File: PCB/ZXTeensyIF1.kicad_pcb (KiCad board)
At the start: 2 copper layers, 222.4 x 72.5 mm, 79 parts, among them Q1 BC213C, Q10 ZTX313, Q11 ZTX313, Q2 BC213C, Q3 BC184C, Q4 PN2222A, Q5 PN2222A, Q6 BC184C, Q9 BC184C, SW1 PTH_RA_h7.5mm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

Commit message: feat: Upload initial PCB v0.3
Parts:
- C3, C4: footprint Resistor_THT:R_Axial_DIN0207_L6.3mm_D2.5mm_P10.16mm_Horizontal -> Capacitor_THT:C_Disc_D3.4mm_W2.1mm_P2.50mm
- Q4, Q5: footprint Package_TO_SOT_THT:TO-92_Inline -> Package_TO_SOT_THT:TO-92_Inline_Wide
- R35: footprint Resistor_THT:R_Axial_DIN0207_L6.3mm_D2.5mm_P10.16mm_Horizontal -> Resistor_THT:R_Axial_DIN0207_L6.3mm_D2.5mm_P7.62mm_Horizontal
- moved C3 10.5 mm to (150.3, 112.8), turned to -90 degrees
- moved R35 9.34 mm to (143.7, 112.8), turned to -90 degrees
- moved C4 3.61 mm to (147.6, 115.3), turned to -90 degrees
- moved C1 2.24 mm to (124.8, 82.0), turned to -90 degrees
- moved C7 1.46 mm to (96.2, 82.9)
- moved Q5 1.09 mm to (176.6, 115.3)
- moved C8 0.79 mm to (93.6, 94.5)
- moved C13 0.76 mm to (128.1, 95.0)
- moved Q4 0.73 mm to (178.9, 115.3)
- moved X1 0.26 mm to (154.2, 117.7)
- moved C2 0.10 mm to (124.8, 87.7)
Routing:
- net GND: track 867.7 -> 837.8 mm, vias 30 -> 32
- net Net-(C3-Pad1): track 77.5 -> 67.9 mm
- net Net-(U8-VS-): track 27.5 -> 19.1 mm
- net ~{RESET}: track 141.6 -> 135.7 mm
- net ~{NMI}: track 78.0 -> 83.5 mm
- net -5V: track 12.4 -> 7.11 mm
- net Net-(C4-Pad2): track 78.0 -> 72.9 mm
- net DTR_1: track 153.3 -> 149.5 mm
- net D7: track 158.3 -> 161.8 mm
- net +9V: track 143.7 -> 141.1 mm
- net D1: track 189.7 -> 187.2 mm
- net Net-(U8-T1OUT): track 48.0 -> 50.3 mm
- net D2: track 172.0 -> 170.4 mm
- net Net-(U8-VS+): track 22.8 -> 21.4 mm
- net D4: track 168.6 -> 170.0 mm
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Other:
- board text added: "${PRJ_NAME} ${PRJ_REVISION}, CraigE ${PRJ_DATE}"
- board text removed: "ZXTeensyIF1 v0.1, CraigE 2025"

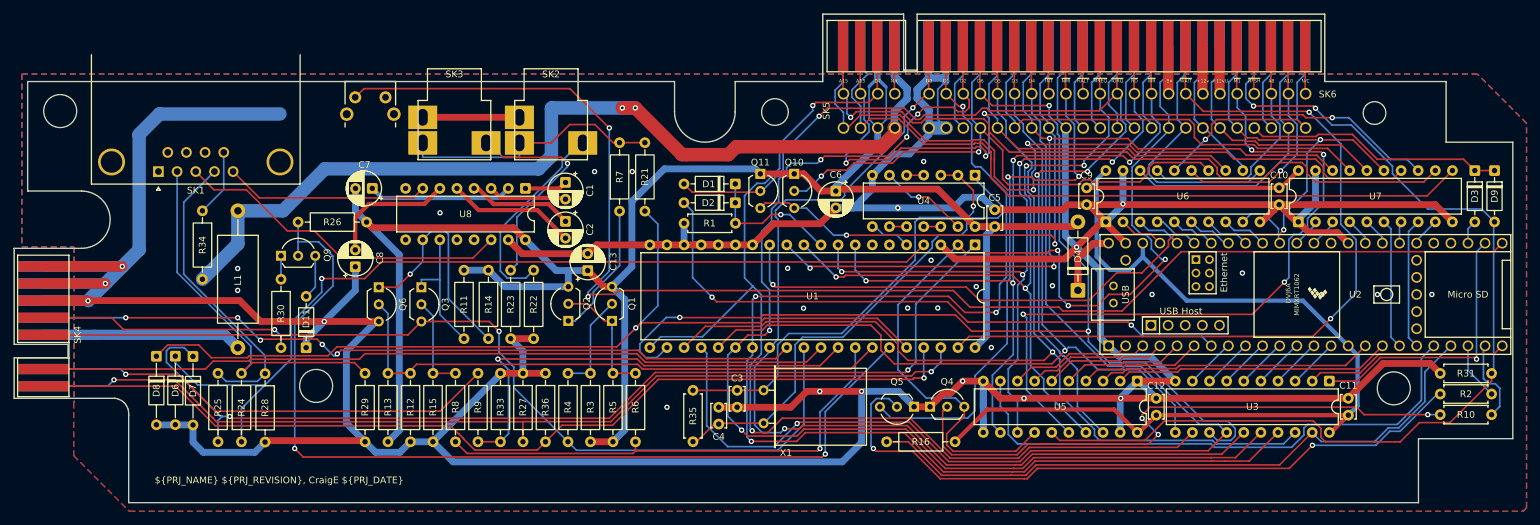
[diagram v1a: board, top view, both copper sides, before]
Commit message: feat: Add ESP-01S header to PCB v0.5
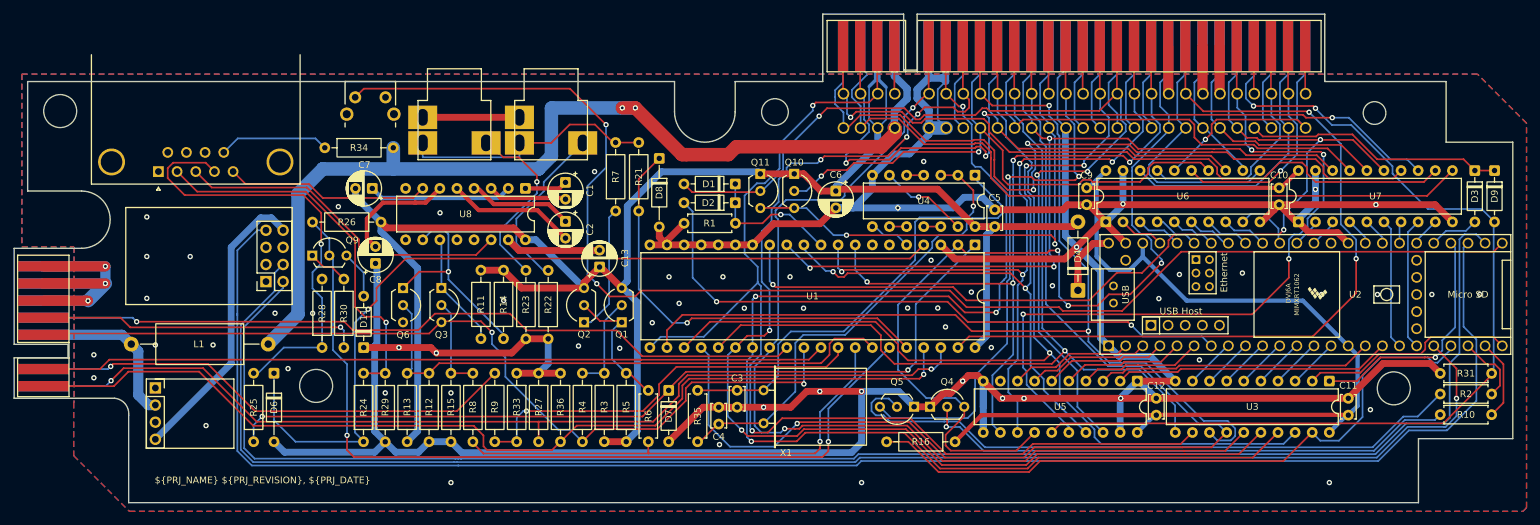
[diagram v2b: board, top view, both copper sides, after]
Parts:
- added J1: ESP-01S-Header, Connector_PinSocket_2.54mm:PinSocket_2x04_P2.54mm_Vertical, F.Cu at (80.4, 96.7)
- added J3: Polou D24V5F3, Connector_PinSocket_2.54mm:PinSocket_1x04_P2.54mm_Vertical, F.Cu at (64.0, 112.5)
- D7: footprint Diode_THT:D_DO-35_SOD27_P10.16mm_Horizontal -> Diode_THT:D_DO-35_SOD27_P7.62mm_Horizontal
- R6: footprint Resistor_THT:R_Axial_DIN0207_L6.3mm_D2.5mm_P10.16mm_Horizontal -> Resistor_THT:R_Axial_DIN0207_L6.3mm_D2.5mm_P7.62mm_Horizontal
- moved D8 80.2 mm to (138.7, 78.4)
- moved D7 70.8 mm to (140.1, 112.8)
- moved R34 20.4 mm to (89.1, 76.8), turned to 0 degrees
- moved L1 20.3 mm to (80.7, 106.0), turned to 180 degrees
- moved R24 18.1 mm to (94.8, 120.4)
- moved D6 14.9 mm to (81.6, 110.3)
- moved R30 9.33 mm to (91.9, 96.3)
- moved R28 9.30 mm to (88.7, 106.5), turned to 90 degrees
- moved D11 8.53 mm to (94.9, 106.5)
- moved R25 5.28 mm to (78.5, 120.4)
- moved Q9 4.64 mm to (87.2, 92.8)
- moved Q6 3.60 mm to (100.7, 97.6)
- moved R6 3.16 mm to (137.1, 112.8)
- moved C8 3.04 mm to (96.6, 94.0)
- moved R29 3.00 mm to (98.1, 110.3)
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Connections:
- net Net-(SK4-Pin_B4) renamed +9V0
- U2 pad 20: TIN_A -> TEPD
- U2 pad 26: TDDir -> TERX
- U2 pad 27: Net-(D3-A) -> TETX
- U2 pad 28: unconnected-(U2-36_CS-Pad28) -> TDDir
- U2 pad 29: unconnected-(U2-37_CS-Pad29) -> Net-(D3-A)
- U5 pad 9: TIN_A -> unconnected-(U5-A8-Pad9)
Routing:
- net TETX: track 0.00 -> 248.5 mm
- net TERX: track 0.00 -> 240.9 mm
- net TEPD: track 0.00 -> 225.9 mm, vias 0 -> 1
- net GND: track 837.8 -> 726.8 mm, vias 32 -> 65
- net TIN_A: track 82.8 -> 0.00 mm
- net NET36: track 136.5 -> 64.6 mm
- net Net-(J1-Pin_8): track 0.00 -> 43.5 mm
- net DTR_1: track 149.5 -> 125.8 mm
- net Net-(R25-Pad2): track 44.8 -> 67.5 mm, vias 0 -> 1
- net ERASE_35: track 141.1 -> 127.3 mm
- net Net-(SK4-Pin_A5): track 38.1 -> 47.9 mm
- net Net-(Q4-B): track 88.9 -> 80.0 mm, vias 3 -> 1
- net D6: track 163.8 -> 155.3 mm, vias 3 -> 2
- net WRPROT_32: track 68.8 -> 60.4 mm
- net Net-(Q5-B): track 102.6 -> 95.7 mm, vias 2 -> 0
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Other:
- board text added: "${PRJ_NAME} ${PRJ_REVISION}, ${PRJ_DATE}"
- board text removed: "${PRJ_NAME} ${PRJ_REVISION}, CraigE ${PRJ_DATE}"

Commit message: Add silkscreen text
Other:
- board text added: "3V3"
- board text added: "ESP-01S"
- board text added: "GND"
- board text added: "VIN"
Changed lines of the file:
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@@
 		)
 	)
-	(property "PRJ_DATE" "2026-02-05")
+	(property "PRJ_DATE" "2026-02-08")
 	(property "PRJ_NAME" "ZXTeensyIF1")
 	(property "PRJ_REVISION" "v0.5")
@@
 		(layer "Edge.Cuts")
 	)
+	(gr_text "3V3"
+		(at 65.8114 120.6754 0)
+		(layer "F.SilkS")
+		(effects
+			(font
+				(size 1 1)
+				(thickness 0.15)
+			)
+			(justify left bottom)
+		)
+	)
+	(gr_text "VIN"
+		(at 65.8114 115.5954 0)
+		(layer "F.SilkS")
+		(effects
+			(font
+				(size 1 1)
+				(thickness 0.15)
+			)
+			(justify left bottom)
+		)
+	)
+	(gr_text "GND"
+		(at 65.8114 118.1354 0)
+		(layer "F.SilkS")
+		(effects
+			(font
+				(size 1 1)
+				(thickness 0.15)
+			)
+			(justify left bottom)
+		)
+	)
+	(gr_text "ESP-01S"
+		(locked yes)
+		(at 68.51071 89.66955 0)
+		(layer "F.SilkS")
+		(effects
+			(font
+				(size 1 1)
+				(thickness 0.15)
+			)
+			(justify left bottom)
+		)
+	)
 	(gr_text "${PRJ_NAME} ${PRJ_REVISION}, ${PRJ_DATE}"
 		(at 63.8556 126.746 0)
@@
 	(group ""
 		(locked yes)
-		(members "d820edde-8ae0-4da0-8973-3ad2fe5a2ae9" "de12b274-2a6e-492c-b6fc-8a5622de27ed")
+		(members "d820edde-8ae0-4da0-8973-3ad2fe5a2ae9" "de12b274-2a6e-492c-b6fc-8a5622de27ed"
+			"e628a1bc-3ac2-4b91-a549-73b6a515b474"
+		)
+	)
+	(group ""
+		(members "3c47943e-7347-4d15-bad2-3ed72209b964" "80866c92-00ea-4d94-bf1f-d6b2a7ca4847"
+			"d6e526b1-69ad-4888-899b-9402fcfd270b"
+		)
 	)
 	(embedded_fonts no)

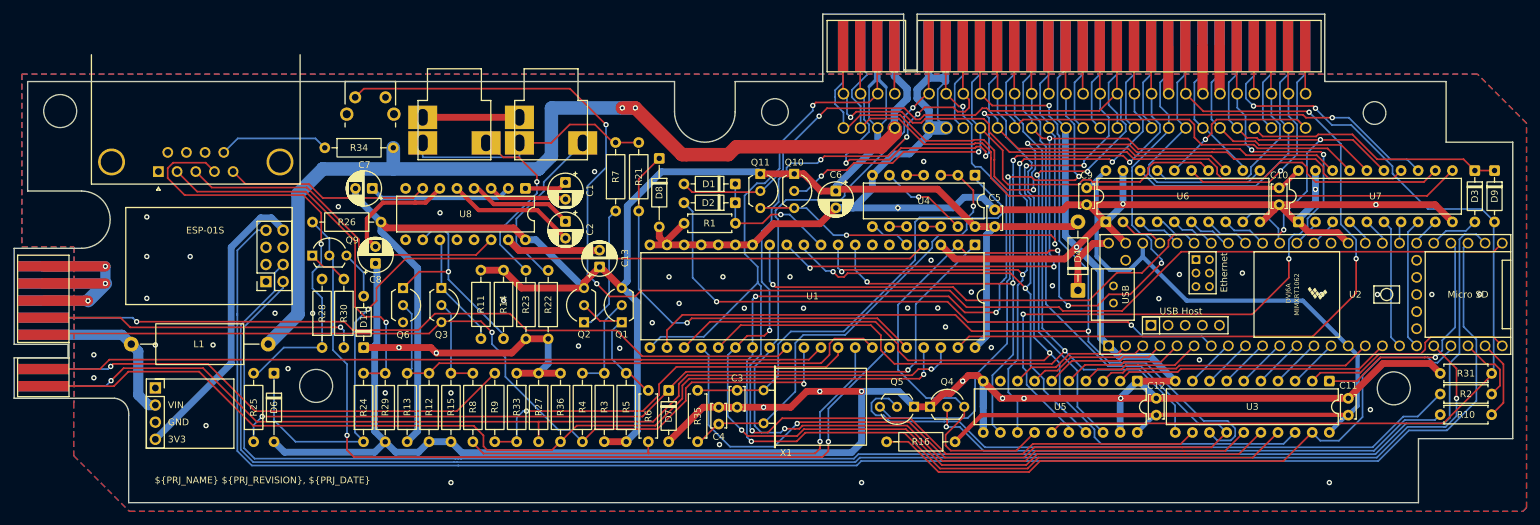
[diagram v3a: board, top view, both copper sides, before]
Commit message: Use active DTR and TXDATA from MAX232
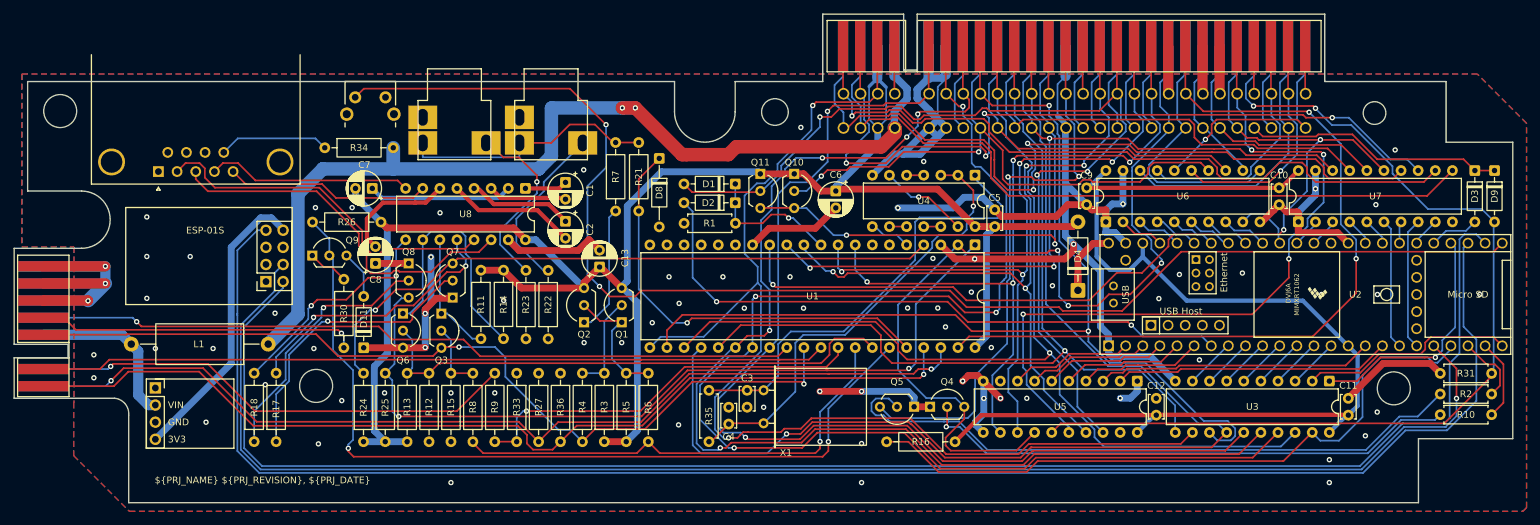
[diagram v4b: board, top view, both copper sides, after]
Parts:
- removed D6: BZX79CV4V3, Diode_THT:D_DO-35_SOD27_P10.16mm_Horizontal
- removed D7: BZX79CV4V3, Diode_THT:D_DO-35_SOD27_P7.62mm_Horizontal
- removed R28, R29: 6K8, Resistor_THT:R_Axial_DIN0207_L6.3mm_D2.5mm_P10.16mm_Horizontal
- added Q7: PN2222A, Package_TO_SOT_THT:TO-92_Inline_Wide, F.Cu at (108.1, 99.1)
- added Q8: PN2222A, Package_TO_SOT_THT:TO-92_Inline_Wide, F.Cu at (101.5, 94.0)
- added R17: 6K8, Resistor_THT:R_Axial_DIN0207_L6.3mm_D2.5mm_P10.16mm_Horizontal, F.Cu at (81.9, 120.4)
- added R18: 6K8, Resistor_THT:R_Axial_DIN0207_L6.3mm_D2.5mm_P10.16mm_Horizontal, F.Cu at (78.6, 120.4)
- R24: value 4K7 -> 1K0
- R25: value 10K -> 1K0
- R6: footprint Resistor_THT:R_Axial_DIN0207_L6.3mm_D2.5mm_P7.62mm_Horizontal -> Resistor_THT:R_Axial_DIN0207_L6.3mm_D2.5mm_P10.16mm_Horizontal
- moved R25 22.0 mm to (98.1, 110.3), turned to -90 degrees
- moved Q3 3.80 mm to (106.4, 101.4)
- moved Q6 3.78 mm to (100.7, 101.4)
- moved R6 2.54 mm to (137.1, 110.3)
- moved R35 1.68 mm to (146.1, 112.8)
- moved C3 1.48 mm to (151.8, 112.8)
- moved C4 1.48 mm to (149.0, 115.3)
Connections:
- R24 pad 1: TXDATA_4 -> +5V
- R24 pad 2: Net-(R24-Pad2) -> TXDATA_4
- R25 pad 2: Net-(R25-Pad2) -> +5V
- SK1 pad 2: Net-(R24-Pad2) -> Net-(U8-R1IN)
- SK1 pad 4: Net-(R25-Pad2) -> Net-(U8-R2IN)
- U2 pad 52: unconnected-(U2-GND-Pad52) -> GND
- U2 pad 58: unconnected-(U2-GND-Pad58) -> GND
- U2 pad 59: unconnected-(U2-GND-Pad59) -> GND
- U8 pad 12: unconnected-(U8-R1OUT-Pad12) -> Net-(U8-R1OUT)
- U8 pad 13: unconnected-(U8-R1IN-Pad13) -> Net-(U8-R1IN)
- U8 pad 8: unconnected-(U8-R2IN-Pad8) -> Net-(U8-R2IN)
- U8 pad 9: unconnected-(U8-R2OUT-Pad9) -> Net-(U8-R2OUT)
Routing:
- net GND: track 726.8 -> 399.2 mm, vias 65 -> 76
- net Net-(R25-Pad2): track 67.5 -> 0.00 mm, vias 1 -> 0
- net Net-(R24-Pad2): track 56.9 -> 0.00 mm, vias 1 -> 0
- net Net-(U8-R1IN): track 0.00 -> 53.1 mm
- net Net-(Q7-B): track 0.00 -> 42.8 mm, vias 0 -> 1
- net Net-(U8-R1OUT): track 0.00 -> 40.5 mm, vias 0 -> 2
- net Net-(Q8-B): track 0.00 -> 38.4 mm, vias 0 -> 1
- net Net-(U8-R2OUT): track 0.00 -> 33.8 mm, vias 0 -> 2
- net TXDATA_4: track 130.1 -> 97.0 mm
- net Net-(U8-R2IN): track 0.00 -> 30.4 mm
- net D0: track 149.7 -> 161.8 mm
- net D1: track 186.8 -> 197.2 mm
- net D2: track 169.7 -> 180.1 mm
- net D7: track 162.2 -> 170.5 mm
- net Net-(Q6-C): track 31.4 -> 37.5 mm, vias 1 -> 0
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
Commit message: fix: Minor PCB tweak
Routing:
- net GND: track 399.2 -> 398.2 mm
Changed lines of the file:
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@@
-	)
-	(segment
-		(start 205.0119 86.1131)
-		(end 205.9588 85.1662)
-		(width 1.016)
-		(layer "B.Cu")
-		(net 2)
 	)
 	(segment
@@
 	)
 	(segment
-		(start 205.0119 87.8282)
-		(end 205.0119 86.1131)
-		(width 1.016)
-		(layer "B.Cu")
-		(net 2)
-	)
-	(segment
 		(start 199.0104 82.125)
 		(end 199.0002 82.125)
@@
 	)
 	(segment
+		(start 206.525 81.2351)
+		(end 207.5519 80.2082)
+		(width 1.016)
+		(layer "B.Cu")
+		(net 2)
+	)
+	(segment
 		(start 178.708 66.4781)
 		(end 177.01 68.1759)
@@
 	)
 	(segment
+		(start 205.0119 85.6524)
+		(end 206.525 84.1393)
+		(width 1.016)
+		(layer "B.Cu")
+		(net 2)
+	)
+	(segment
 		(start 176.5554 115.2652)
 		(end 176.5554 113.8554)
@@
 	)
 	(segment
-		(start 205.9588 85.1662)
-		(end 207.5519 85.1662)
+		(start 205.0119 87.8282)
+		(end 205.0119 85.6524)
 		(width 1.016)
 		(layer "B.Cu")
@@
 	)
 	(segment
+		(start 206.525 84.1393)
+		(end 206.525 81.2351)
+		(width 1.016)
+		(layer "B.Cu")
+		(net 2)
+	)
+	(segment
 		(start 186.9 116.275)
 		(end 185.65 117.525)
@@
 		(width 1.016)
 		(layer "B.Cu")
-		(net 2)
-	)
-	(segment
-		(start 207.5519 85.1662)
-		(end 207.5519 80.2082)
-		(width 1.016)
-		(layer "B.Cu")
